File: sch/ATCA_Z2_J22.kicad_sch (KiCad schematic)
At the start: 1 part, among them J22 TE_64690XX-1_J22

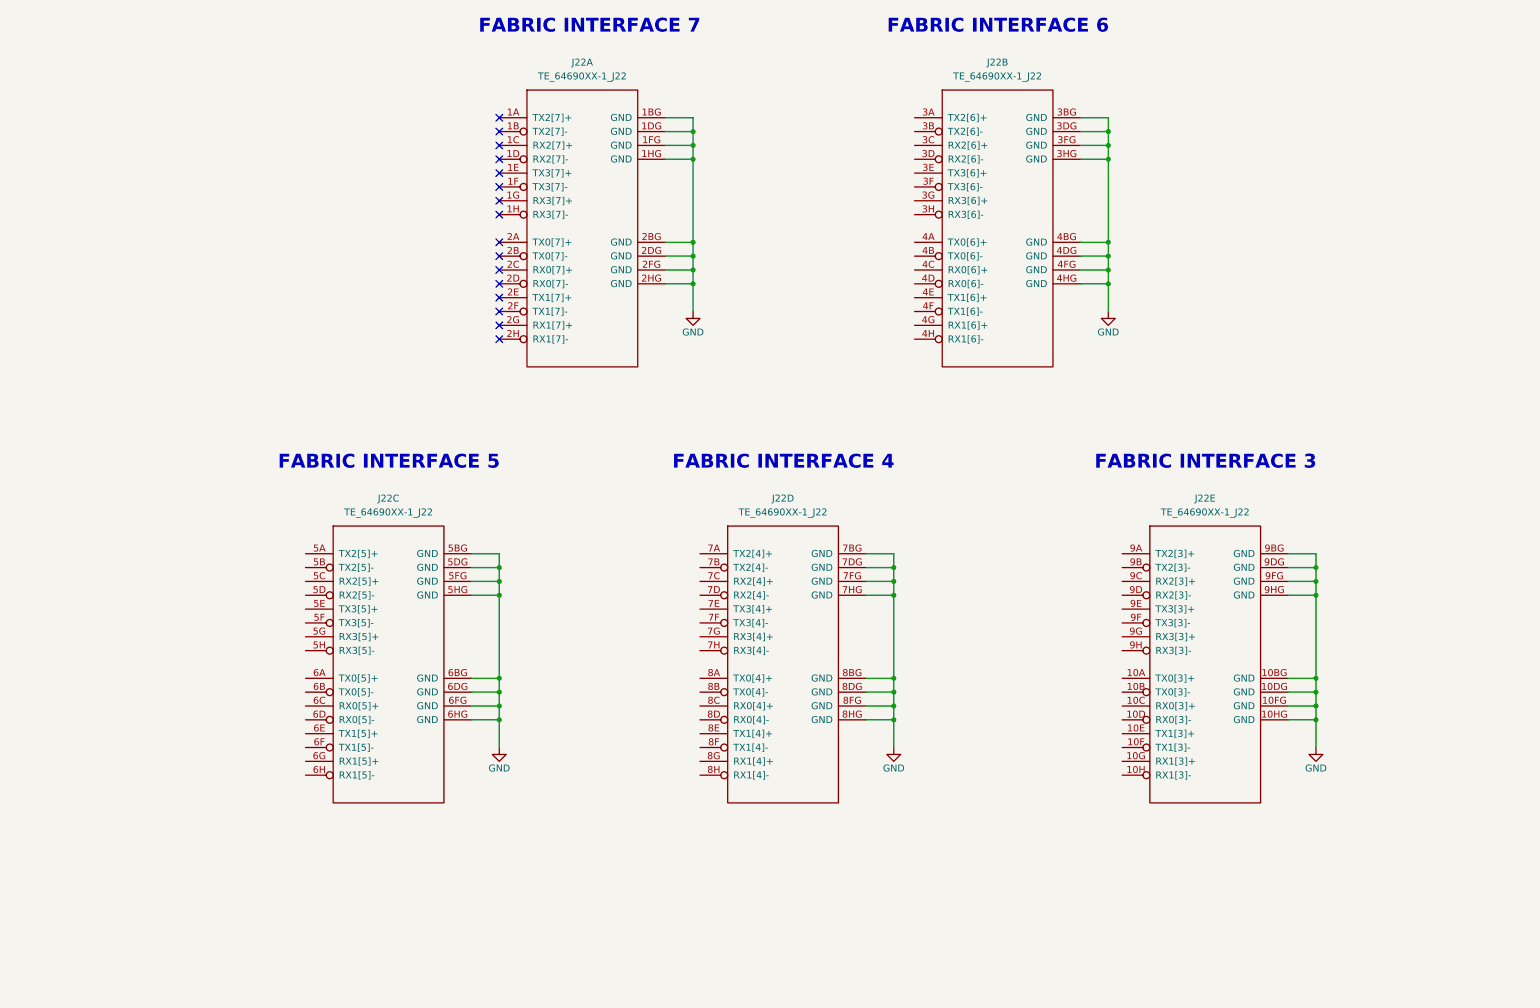
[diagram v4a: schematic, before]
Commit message: adding clks and fiber sheets
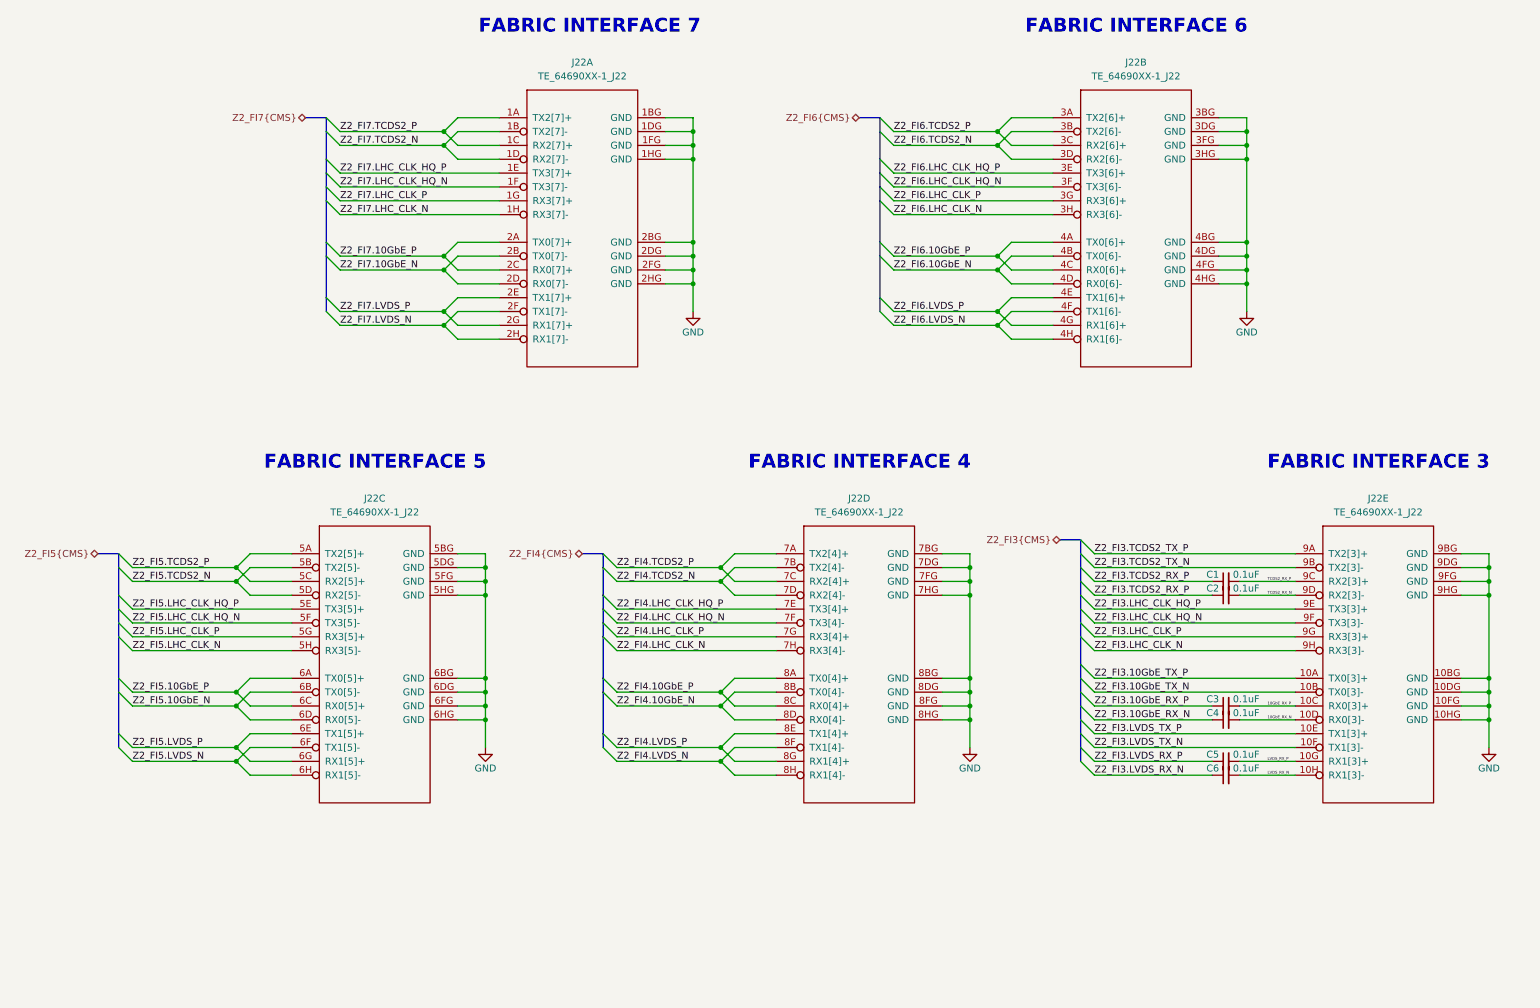
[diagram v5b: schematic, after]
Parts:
- added C1, C2, C3, C4, C5, C6: 0.1uF, Capacitor_SMD:C_0402_1005Metric, symbol Device:C_Small
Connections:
- net Z2_FI6.TCDS2_P: now reaches J22.3A (TX2[6]+)
- net Z2_FI6.TCDS2_P: now also J22.3C (RX2[6]+)
- net Z2_FI6.TCDS2_N: now reaches J22.3B (TX2[6]-)
- net Z2_FI6.TCDS2_N: now also J22.3D (RX2[6]-)
- net Z2_FI6.LHC_CLK_HQ_P: now reaches J22.3E (TX3[6]+)
- net Z2_FI6.LHC_CLK_HQ_N: now reaches J22.3F (TX3[6]-)
- net Z2_FI6.LHC_CLK_P: now reaches J22.3G (RX3[6]+)
- net Z2_FI6.LHC_CLK_N: now reaches J22.3H (RX3[6]-)
- net Z2_FI6.10GbE_P: now reaches J22.4A (TX0[6]+)
- net Z2_FI6.10GbE_P: now also J22.4C (RX0[6]+)
- net Z2_FI6.10GbE_N: now reaches J22.4B (TX0[6]-)
- net Z2_FI6.10GbE_N: now also J22.4D (RX0[6]-)
- net Z2_FI6.LVDS_P: now reaches J22.4E (TX1[6]+)
- net Z2_FI6.LVDS_P: now also J22.4G (RX1[6]+)
- net Z2_FI6.LVDS_N: now reaches J22.4F (TX1[6]-)
- net Z2_FI6.LVDS_N: now also J22.4H (RX1[6]-)
- net Z2_FI5.TCDS2_P: now reaches J22.5A (TX2[5]+)
- net Z2_FI5.TCDS2_P: now also J22.5C (RX2[5]+)
- net Z2_FI5.TCDS2_N: now reaches J22.5B (TX2[5]-)
- net Z2_FI5.TCDS2_N: now also J22.5D (RX2[5]-)
- net Z2_FI5.LHC_CLK_HQ_P: now reaches J22.5E (TX3[5]+)
- net Z2_FI5.LHC_CLK_HQ_N: now reaches J22.5F (TX3[5]-)
- net Z2_FI5.LHC_CLK_P: now reaches J22.5G (RX3[5]+)
- net Z2_FI5.LHC_CLK_N: now reaches J22.5H (RX3[5]-)
- net Z2_FI5.10GbE_P: now reaches J22.6A (TX0[5]+)
- net Z2_FI5.10GbE_P: now also J22.6C (RX0[5]+)
- net Z2_FI5.10GbE_N: now reaches J22.6B (TX0[5]-)
- net Z2_FI5.10GbE_N: now also J22.6D (RX0[5]-)
- net Z2_FI5.LVDS_P: now reaches J22.6E (TX1[5]+)
- net Z2_FI5.LVDS_P: now also J22.6G (RX1[5]+)
- net Z2_FI5.LVDS_N: now reaches J22.6F (TX1[5]-)
- net Z2_FI5.LVDS_N: now also J22.6H (RX1[5]-)
- net Z2_FI4.TCDS2_P: now reaches J22.7A (TX2[4]+)
- net Z2_FI4.TCDS2_P: now also J22.7C (RX2[4]+)
- net Z2_FI4.TCDS2_N: now reaches J22.7B (TX2[4]-)
- net Z2_FI4.TCDS2_N: now also J22.7D (RX2[4]-)
- net Z2_FI4.LHC_CLK_HQ_P: now reaches J22.7E (TX3[4]+)
- net Z2_FI4.LHC_CLK_HQ_N: now reaches J22.7F (TX3[4]-)
- net Z2_FI4.LHC_CLK_P: now reaches J22.7G (RX3[4]+)
- net Z2_FI4.LHC_CLK_N: now reaches J22.7H (RX3[4]-)
- net Z2_FI4.10GbE_P: now reaches J22.8A (TX0[4]+)
- net Z2_FI4.10GbE_P: now also J22.8C (RX0[4]+)
- net Z2_FI4.10GbE_N: now reaches J22.8B (TX0[4]-)
- net Z2_FI4.10GbE_N: now also J22.8D (RX0[4]-)
- net Z2_FI4.LVDS_P: now reaches J22.8E (TX1[4]+)
- net Z2_FI4.LVDS_P: now also J22.8G (RX1[4]+)
- net Z2_FI4.LVDS_N: now reaches J22.8F (TX1[4]-)
- net Z2_FI4.LVDS_N: now also J22.8H (RX1[4]-)
- net Z2_FI3.10GbE_TX_P: now reaches J22.10A (TX0[3]+)
- net Z2_FI3.10GbE_TX_N: now reaches J22.10B (TX0[3]-)
- net 10GbE_RX_P: now reaches J22.10C (RX0[3]+)
- net 10GbE_RX_P: now also C3.2
- net 10GbE_RX_N: now reaches J22.10D (RX0[3]-)
- net 10GbE_RX_N: now also C4.2
- net Z2_FI3.LVDS_TX_P: now reaches J22.10E (TX1[3]+)
- net Z2_FI3.LVDS_TX_N: now reaches J22.10F (TX1[3]-)
- net LVDS_RX_P: now reaches J22.10G (RX1[3]+)
- net LVDS_RX_P: now also C5.2
- net LVDS_RX_N: now reaches J22.10H (RX1[3]-)
- net LVDS_RX_N: now also C6.2
- net Z2_FI3.TCDS2_TX_P: now reaches J22.9A (TX2[3]+)
- net Z2_FI3.TCDS2_TX_N: now reaches J22.9B (TX2[3]-)
- net TCDS2_RX_P: now reaches J22.9C (RX2[3]+)
- net TCDS2_RX_P: now also C1.2
- net TCDS2_RX_N: now reaches J22.9D (RX2[3]-)
- net TCDS2_RX_N: now also C2.2
- net Z2_FI3.LHC_CLK_HQ_P: now reaches J22.9E (TX3[3]+)
- net Z2_FI3.LHC_CLK_HQ_N: now reaches J22.9F (TX3[3]-)
- net Z2_FI3.LHC_CLK_P: now reaches J22.9G (RX3[3]+)
- net Z2_FI3.LHC_CLK_N: now reaches J22.9H (RX3[3]-)
- net Z2_FI7.TCDS2_P: now reaches J22.1A (TX2[7]+)
- net Z2_FI7.TCDS2_P: now also J22.1C (RX2[7]+)
- net Z2_FI7.TCDS2_N: now reaches J22.1B (TX2[7]-)
- net Z2_FI7.TCDS2_N: now also J22.1D (RX2[7]-)
- net Z2_FI7.LHC_CLK_HQ_P: now reaches J22.1E (TX3[7]+)
- net Z2_FI7.LHC_CLK_HQ_N: now reaches J22.1F (TX3[7]-)
- net Z2_FI7.LHC_CLK_P: now reaches J22.1G (RX3[7]+)
- net Z2_FI7.LHC_CLK_N: now reaches J22.1H (RX3[7]-)
- net Z2_FI7.10GbE_P: now reaches J22.2A (TX0[7]+)
- net Z2_FI7.10GbE_P: now also J22.2C (RX0[7]+)
- net Z2_FI7.10GbE_N: now reaches J22.2B (TX0[7]-)
- net Z2_FI7.10GbE_N: now also J22.2D (RX0[7]-)
- net Z2_FI7.LVDS_P: now reaches J22.2E (TX1[7]+)
- net Z2_FI7.LVDS_P: now also J22.2G (RX1[7]+)
- net Z2_FI7.LVDS_N: now reaches J22.2F (TX1[7]-)
- net Z2_FI7.LVDS_N: now also J22.2H (RX1[7]-)
- new net Z2_FI3.10GbE_RX_N: C4.1
- new net Z2_FI3.10GbE_RX_P: C3.1
- new net Z2_FI3.LVDS_RX_N: C6.1
- new net Z2_FI3.LVDS_RX_P: C5.1
- new net Z2_FI3.TCDS2_RX_P: C1.1, C2.1
- no-connect marks 16 -> 0
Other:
- moved on the sheet: J22B, J22C, J22D, J22E

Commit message: sfp+ sheet
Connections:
- net Z2_FI3.TCDS2_RX_P: no longer C2.1
- new net Z2_FI3.TCDS2_RX_N: C2.1
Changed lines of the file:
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@@
     (effects (font (size 0.5 0.5)) (justify left bottom))
   )
-  (label "Z2_FI3.TCDS2_RX_P" (at 209.55 121.92 0) (fields_autoplaced)
+  (label "Z2_FI3.TCDS2_RX_N" (at 209.55 121.92 0) (fields_autoplaced)
     (effects (font (size 1.27 1.27)) (justify left bottom))
   )

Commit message: sch work
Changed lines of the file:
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@@
   (title_block
     (title "ATCA Simple Loopback HUB")
-    (date "2023-09-12")
+    (date "2023-09-26")
     (rev "1.0")
     (company "Karlsruhe Institute of Technology (KIT)")
@@
     (stroke (width 0) (type default))
   )
+  (text_box "NOTES:\n1) Fabric Interface (FI) 3 is the only one that is broken out to the front panel\n2) FI3 has capacitors at the RX channel since the TX channel has capacitors at the receiving RX channel in the slot board"
+    (at 13.97 181.61 0) (size 161.29 13.97)
+    (stroke (width 0) (type default))
+    (fill (type none))
+    (effects (font (size 1.27 1.27)) (justify left top))
+  )
   (text "FABRIC INTERFACE 3" (at 241.3 99.06 0)
